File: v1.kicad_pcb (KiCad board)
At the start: 4 copper layers, 223.5 x 132.1 mm, 463 parts, among them CN1 ARJM11D7-502-AB-EW2, J1 Powerpole G1377G2, J10 Barrel_Jack, J11 USB_A, J2 Conn_01x02, J3 Conn_01x02, J4 Conn_01x02, J5 Conn_01x02, J6 Conn_01x02, J7 Conn_01x02, J8 Micro_SD_Card_Det, J9 USB_B_Micro, M1 Logo_10mmx10mm, Q1 Si7141DP, Q10 Si7141DP, Q11 SI1539CDL-T1-GE3, Q12 SI1539CDL-T1-GE3, Q13 SI1539CDL-T1-GE3, Q15 Si7141DP, Q16 SI1539CDL-T1-GE3, Q17 Si7141DP, Q18 SI1539CDL-T1-GE3, Q19 Si7141DP, Q2 SI1539CDL-T1-GE3, Q20 SI1539CDL-T1-GE3, Q21 SI1539CDL-T1-GE3, Q3 SI1539CDL-T1-GE3, Q5 Si7141DP, Q6 SI1539CDL-T1-GE3, Q7 Si7141DP, Q8 SI1539CDL-T1-GE3, SW1 SW_SPDT, SW2 SW_Push, T1 Transformer_SP_1S, U1 171050601, U10 74HC08BQ, U11 TLV803, U12 TLV803, U13 74HC74, U14 74HC74, U15 MAX9612, U16 74HC1G08, U17 TPS3701DDCR, U18 NCP1117-3.3_TO252, U19 74HC08BQ, U2 TLV803, U20 TLV803, U21 TLV803, U22 74HC74, U23 74HC74, U24 MAX9612, U25 74HC1G08, U26 TPS3701DDCR, U27 NCP1117-3.3_TO252, U28 TLV803S, U29 74HC08BQ, U3 TLV803, U30 TLV803, U31 TLV803, U32 74HC74, U33 74HC74, U34 MAX9612, U35 74HC1G08, U36 TPS3701DDCR, U37 TLV803, U38 TLV803, U39 74HC74, U4 74HC74, U40 74HC74, U41 MAX9612, U42 74HC1G08, U43 TPS3701DDCR, U44 LT3460, U45 TLV803, U46 TLV803, U47 74HC74, U48 74HC74, U49 MAX9612, U5 74HC74, U50 74HC1G08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

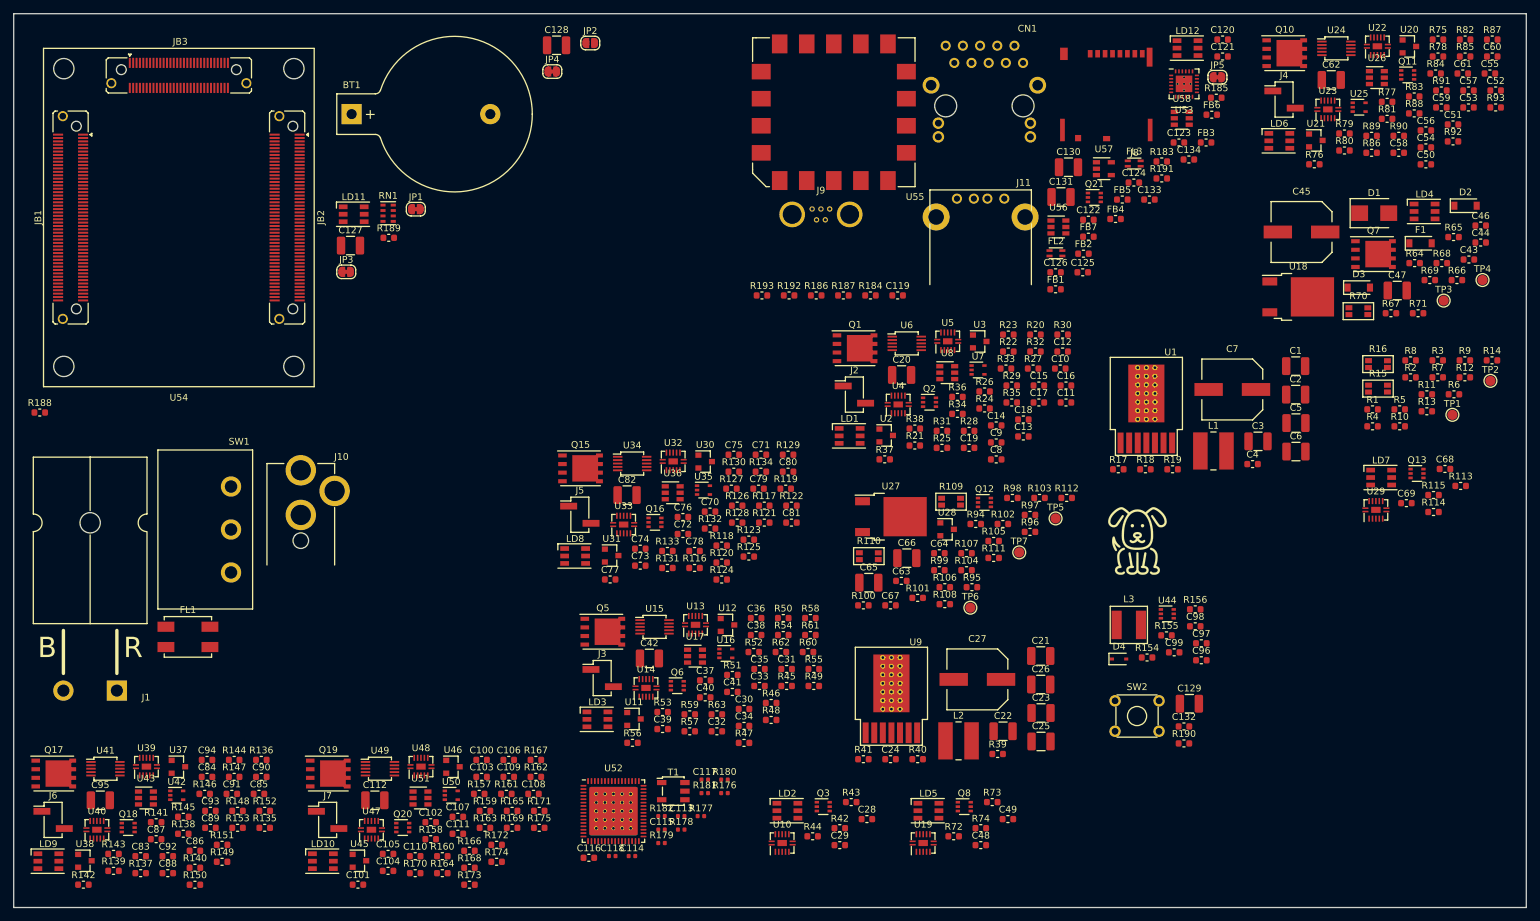
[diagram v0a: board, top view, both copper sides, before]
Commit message: Implemented FPGA based PMIC
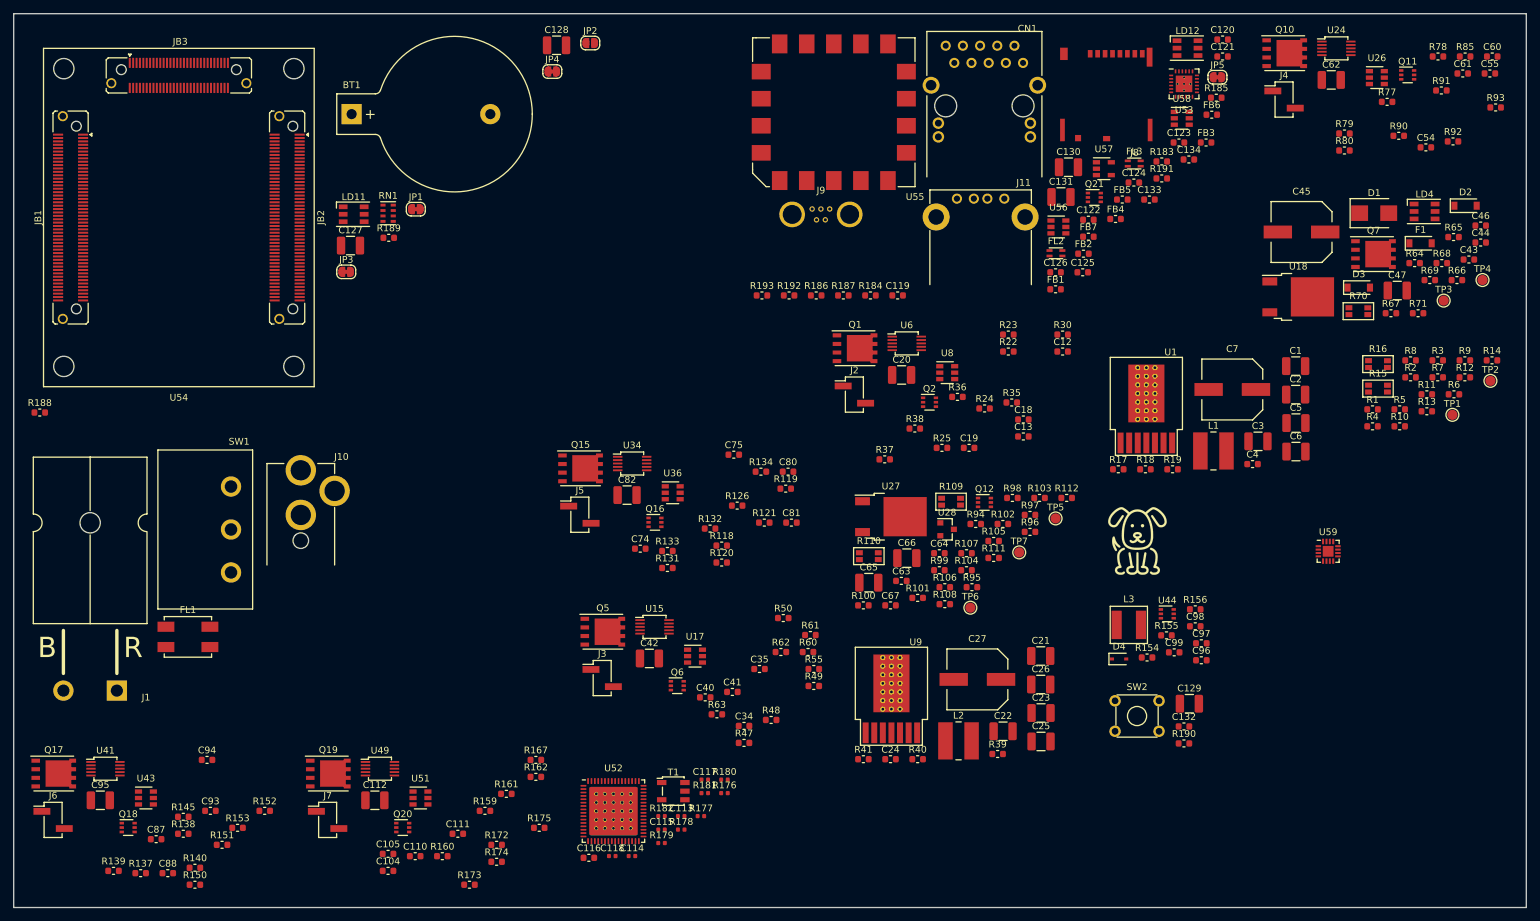
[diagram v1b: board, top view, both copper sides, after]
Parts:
- removed C10, C102, C103, C107, C109, C11, C15, C17, C29, C32, C33, C37, C39, C49, C52, C53, C57, C59, C69, C72, C73, C77, C79, C85, C86, C90, C92: 100n, Capacitor_SMD:C_0603_1608Metric
- removed C100, C101, C106, C14, C30, C31, C36, C50, C51, C56, C70, C71, C76, C8, C83, C84, C89, C9: 1u, Capacitor_SMD:C_0603_1608Metric
- removed C108, C16, C38, C58, C78, C91: 100nF, Capacitor_SMD:C_0603_1608Metric
- removed C28, C48, C68: 4u7, Capacitor_SMD:C_0603_1608Metric
- removed LD1, LD10, LD2, LD3, LD5, LD6, LD7, LD8, LD9: LED_Cree_CLX6E-FKC, LED_SMD:LED_RGB_PLCC-6
- removed Q13, Q3, Q8: SI1539CDL-T1-GE3, Package_TO_SOT_SMD:SOT-363_SC-70-6
- removed R113, R42, R72: 100k, Resistor_SMD:R_0603_1608Metric
- removed R114, R125, R144, R166, R29, R43, R54, R73, R84: 22k, Resistor_SMD:R_0603_1608Metric
- removed R115, R130, R149, R171, R34, R44, R59, R74, R89: 33k, Resistor_SMD:R_0603_1608Metric
- removed R116, R117, R122, R123, R127, R128, R129, R135, R136, R141, R142, R146, R147, R148, R157, R158, R163, R164, R168, R169, R170, R20, R21, R26, R27, R31, R32, R33, R45, R46, R51, R52, R56, R57, R58, R75, R76, R81, R82, R86, R87, R88: 47k, Resistor_SMD:R_0603_1608Metric
- removed R124, R143, R165, R28, R53, R83: 7k5, Resistor_SMD:R_0603_1608Metric
- removed U10, U19, U29: 74HC08BQ, IC_WUT:DHVQFN14_(SOT762-1)
- removed U11, U12, U2, U20, U21, U3, U30, U31, U37, U38, U45, U46: TLV803, Package_TO_SOT_SMD:SOT-23
- removed U13, U14, U22, U23, U32, U33, U39, U4, U40, U47, U48, U5: 74HC74, IC_WUT:DHVQFN14_(SOT762-1)
- removed U16, U25, U35, U42, U50, U7: 74HC1G08, Package_TO_SOT_SMD:SOT-353_SC-70-5
- added U59: AD5689RxCPZ, Package_CSP:LFCSP-16-1EP_3x3mm_P0.5mm_EP1.854x1.854mm, F.Cu at (242.5, 115.0)
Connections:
- R126 pad 2: /Power Supply/Stage 3 Regulators/1V8 Monitor/~Overcurrent -> /Power Supply/Stage 3 Regulators/1V8 Monitor/I_Good
- R134 pad 2: /Power Supply/Stage 3 Regulators/1V8 Monitor/~V_Fault -> /Power Supply/Stage 3 Regulators/1V8 Monitor/V_Good
- R145 pad 2: /Power Supply/Stage 3 Regulators/ADC 3V3 Monitor/~Overcurrent -> /Power Supply/Stage 3 Regulators/ADC 3V3 Monitor/I_Good
- R153 pad 2: /Power Supply/Stage 3 Regulators/ADC 3V3 Monitor/~V_Fault -> /Power Supply/Stage 3 Regulators/ADC 3V3 Monitor/V_Good
- R167 pad 2: /Power Supply/Stage 3 Regulators/16V Monitor/~Overcurrent -> /Power Supply/Stage 3 Regulators/16V Monitor/I_Good
- R175 pad 2: /Power Supply/Stage 3 Regulators/16V Monitor/~V_Fault -> /Power Supply/Stage 3 Regulators/16V Monitor/V_Good
- R30 pad 2: /Power Supply/Stage 2 Regulators/3V3 Monitor/~Overcurrent -> /Power Supply/Stage 2 Regulators/3V3 Monitor/I_Good
- R38 pad 2: /Power Supply/Stage 2 Regulators/3V3 Monitor/~V_Fault -> /Power Supply/Stage 2 Regulators/3V3 Monitor/V_Good
- R55 pad 2: /Power Supply/Stage 2 Regulators/5V Monitor/~Overcurrent -> /Power Supply/Stage 2 Regulators/5V Monitor/I_Good
- R63 pad 2: /Power Supply/Stage 2 Regulators/5V Monitor/~V_Fault -> /Power Supply/Stage 2 Regulators/5V Monitor/V_Good
- R85 pad 2: /Power Supply/Stage 1 Regulators/12V Monitor/~Overcurrent -> /Power Supply/Stage 1 Regulators/12V Monitor/I_Good
- R93 pad 2: /Power Supply/Stage 1 Regulators/12V Monitor/~V_Fault -> /Power Supply/Stage 1 Regulators/12V Monitor/V_Good
- U15 pad 1: /Power Supply/Stage 2 Regulators/5V Monitor/~Overcurrent -> /Power Supply/Stage 2 Regulators/5V Monitor/I_Good
- U17 pad 1: /Power Supply/Stage 2 Regulators/5V Monitor/~V_Fault -> /Power Supply/Stage 2 Regulators/5V Monitor/V_Good
- U17 pad 6: /Power Supply/Stage 2 Regulators/5V Monitor/~V_Fault -> /Power Supply/Stage 2 Regulators/5V Monitor/V_Good
- U24 pad 1: /Power Supply/Stage 1 Regulators/12V Monitor/~Overcurrent -> /Power Supply/Stage 1 Regulators/12V Monitor/I_Good
- U26 pad 1: /Power Supply/Stage 1 Regulators/12V Monitor/~V_Fault -> /Power Supply/Stage 1 Regulators/12V Monitor/V_Good
- U26 pad 6: /Power Supply/Stage 1 Regulators/12V Monitor/~V_Fault -> /Power Supply/Stage 1 Regulators/12V Monitor/V_Good
- U34 pad 1: /Power Supply/Stage 3 Regulators/1V8 Monitor/~Overcurrent -> /Power Supply/Stage 3 Regulators/1V8 Monitor/I_Good
- U36 pad 1: /Power Supply/Stage 3 Regulators/1V8 Monitor/~V_Fault -> /Power Supply/Stage 3 Regulators/1V8 Monitor/V_Good
- U36 pad 6: /Power Supply/Stage 3 Regulators/1V8 Monitor/~V_Fault -> /Power Supply/Stage 3 Regulators/1V8 Monitor/V_Good
- U41 pad 1: /Power Supply/Stage 3 Regulators/ADC 3V3 Monitor/~Overcurrent -> /Power Supply/Stage 3 Regulators/ADC 3V3 Monitor/I_Good
- U43 pad 1: /Power Supply/Stage 3 Regulators/ADC 3V3 Monitor/~V_Fault -> /Power Supply/Stage 3 Regulators/ADC 3V3 Monitor/V_Good
- U43 pad 6: /Power Supply/Stage 3 Regulators/ADC 3V3 Monitor/~V_Fault -> /Power Supply/Stage 3 Regulators/ADC 3V3 Monitor/V_Good
- U49 pad 1: /Power Supply/Stage 3 Regulators/16V Monitor/~Overcurrent -> /Power Supply/Stage 3 Regulators/16V Monitor/I_Good
- U51 pad 1: /Power Supply/Stage 3 Regulators/16V Monitor/~V_Fault -> /Power Supply/Stage 3 Regulators/16V Monitor/V_Good
- U51 pad 6: /Power Supply/Stage 3 Regulators/16V Monitor/~V_Fault -> /Power Supply/Stage 3 Regulators/16V Monitor/V_Good
- U6 pad 1: /Power Supply/Stage 2 Regulators/3V3 Monitor/~Overcurrent -> /Power Supply/Stage 2 Regulators/3V3 Monitor/I_Good
- U8 pad 1: /Power Supply/Stage 2 Regulators/3V3 Monitor/~V_Fault -> /Power Supply/Stage 2 Regulators/3V3 Monitor/V_Good
- U8 pad 6: /Power Supply/Stage 2 Regulators/3V3 Monitor/~V_Fault -> /Power Supply/Stage 2 Regulators/3V3 Monitor/V_Good
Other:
- net class Default: clearance 0.2 -> 0.0889
- rule trace_clearance: 0.2 -> 0.0889

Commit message: muppet hadn't saved everything :(
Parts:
- removed C104, C110, C87, C93, C96: 4u7, Capacitor_SMD:C_0603_1608Metric
- removed C105, C111, C123, C125, C126, C132, C134, C81, C88, C94: 100n, Capacitor_SMD:C_0603_1608Metric
- removed C112, C127, C128, C129, C82, C95: 22u, Capacitor_SMD:C_1210_3225Metric
- removed C113: 10n, Capacitor_SMD:C_0402_1005Metric
- removed C114: 100n, Capacitor_SMD:C_0402_1005Metric
- removed C115, C117, C118: 8p2, Capacitor_SMD:C_0402_1005Metric
- removed C116: 2u2, Capacitor_SMD:C_0603_1608Metric
- removed C119, C120, C121: 100nF, Capacitor_SMD:C_0603_1608Metric
- removed C122, C124, C133: 1u, Capacitor_SMD:C_0603_1608Metric
- removed C130, C131: 47u, Capacitor_SMD:C_1210_3225Metric
- removed C97: 47n, Capacitor_SMD:C_0603_1608Metric
- removed C98: 22p, Capacitor_SMD:C_0603_1608Metric
- removed C99: 22u, Capacitor_SMD:C_0603_1608Metric
- removed CN1: ARJM11D7-502-AB-EW2, Connector_WUT:Connector_RJ45_Magjack_Abracon_ARJM11D7-502-AB-EW2
- removed Q16, Q18, Q20, Q21: SI1539CDL-T1-GE3, Package_TO_SOT_SMD:SOT-363_SC-70-6
- removed Q17, Q19: Si7141DP, Package_SO:PowerPAK_SO-8_Single
- removed R151, R152, R173, R174, R183, R185, R190, R191: 10k, Resistor_SMD:R_0603_1608Metric
- removed R153, R154, R167, R175: 47k, Resistor_SMD:R_0603_1608Metric
- removed R155: 390k, Resistor_SMD:R_0603_1608Metric
- removed R156, R188, R192: 33k, Resistor_SMD:R_0603_1608Metric
- removed R159, R160, R161, R162: R, Resistor_SMD:R_0603_1608Metric
- removed R172: 100R, Resistor_SMD:R_0603_1608Metric
- removed R176, R177: 10R, Resistor_SMD:R_0402_1005Metric
- removed R178, R179: 35R, Resistor_SMD:R_0402_1005Metric
- removed R180, R181, R182: 5R1, Resistor_SMD:R_0402_1005Metric
- removed R184: 4k7, Resistor_SMD:R_0603_1608Metric
- removed R186, R187: 1k, Resistor_SMD:R_0603_1608Metric
- removed R189, R193: 22k, Resistor_SMD:R_0603_1608Metric
- removed U28: TLV803S, Package_TO_SOT_SMD:SOT-23
- removed U34, U41, U49: MAX9612, IC_WUT:uMAX-10_3x3mm_P0.5mm
- removed U36, U43, U51: TPS3701DDCR, Package_TO_SOT_SMD:SOT-23-6
- removed U44: LT3460, Package_TO_SOT_SMD:SOT-363_SC-70-6
- removed U52: LTC2216, IC_WUT:QFN-64-1EP_9x9mm_P0.5mm_EP7.15x7.15mm
- removed U53: TXS02612, IC_WUT:WQFN-24-1EP_4.1x4.1mm_P0.5mm_EP2.45x2.45mm
- removed U54: TE0720, IC_WUT:Trenz_TE0720
- removed U55: JTAG-SMT3, Misc_WUT:JTAG-SMT3-NC
- removed U56, U58: TPD2S017, Package_TO_SOT_SMD:SOT-23-6
- removed U57: TPS2051B, Package_TO_SOT_SMD:SOT-23-5
- removed U59: AD5689RxCPZ, Package_CSP:LFCSP-16-1EP_3x3mm_P0.5mm_EP1.854x1.854mm
- added C10: 100n, Capacitor_SMD:C_0603_1608Metric, F.Cu at (220.6, 112.9)
- added C11: 4u7, Capacitor_SMD:C_0603_1608Metric, F.Cu at (215.0, 117.6)
- added C14: 10u, Capacitor_SMD:C_1210_3225Metric, F.Cu at (156.0, 129.7)
- added C15: 10u, Capacitor_SMD:C_1210_3225Metric, F.Cu at (156.0, 138.1)
- added C16: 470n, Capacitor_SMD:C_0603_1608Metric, F.Cu at (129.8, 144.9)
- added C17: 22u, Capacitor_SMD:C_1210_3225Metric, F.Cu at (150.4, 140.8)
- added C28: 4u7, Capacitor_SMD:C_0603_1608Metric, F.Cu at (265.2, 47.8)
- added C29: 22u, Capacitor_SMD:C_1210_3225Metric, F.Cu at (252.8, 54.9)
- added C30: 4u7, Capacitor_SMD:C_0603_1608Metric, F.Cu at (190.6, 112.9)
- added C31: 100n, Capacitor_SMD:C_0603_1608Metric, F.Cu at (185.0, 120.1)
- added C32: 100n, Capacitor_SMD:C_0603_1608Metric, F.Cu at (185.0, 117.6)
- added C33: 4u7, Capacitor_SMD:C_0603_1608Metric, F.Cu at (186.5, 113.4)
- added C36: 4u7, Capacitor_SMD:C_0603_1608Metric, F.Cu at (198.8, 85.8)
- added C37: 22u, Capacitor_SMD:C_1210_3225Metric, F.Cu at (173.6, 98.3)
- added C38: 22u, Capacitor_SMD:C_1210_3225Metric, F.Cu at (179.2, 94.7)
- added C39: 100nF, Capacitor_SMD:C_0603_1608Metric, F.Cu at (172.8, 101.6)
- added C48: 4u7, Capacitor_SMD:C_0603_1608Metric, F.Cu at (72.1, 158.5)
- added C49: 22u, Capacitor_SMD:C_1210_3225Metric, F.Cu at (60.9, 154.4)
- added C50: 22p, Capacitor_SMD:C_0603_1608Metric, F.Cu at (147.4, 158.8)
- added C51: 4u7, Capacitor_SMD:C_0603_1608Metric, F.Cu at (147.4, 156.3)
- added C52: 22u, Capacitor_SMD:C_0603_1608Metric, F.Cu at (146.5, 153.8)
- added C53: 47n, Capacitor_SMD:C_0603_1608Metric, F.Cu at (143.4, 157.6)
- added C56: 100n, Capacitor_SMD:C_0603_1608Metric, F.Cu at (187.5, 138.9)
- added C57: 4u7, Capacitor_SMD:C_0603_1608Metric, F.Cu at (183.5, 141.5)
- added C58: 22u, Capacitor_SMD:C_1210_3225Metric, F.Cu at (176.3, 134.8)
- added C59: 2u2, Capacitor_SMD:C_0603_1608Metric, F.Cu at (210.4, 99.0)
- added C68: 100n, Capacitor_SMD:C_0603_1608Metric, F.Cu at (207.2, 130.7)
- added C69: 1u, Capacitor_SMD:C_0603_1608Metric, F.Cu at (178.7, 79.8)
- added C70: 100n, Capacitor_SMD:C_0603_1608Metric, F.Cu at (206.0, 77.0)
- added C71: 1u, Capacitor_SMD:C_0603_1608Metric, F.Cu at (224.4, 53.4)
- added C72: 100n, Capacitor_SMD:C_0603_1608Metric, F.Cu at (212.5, 65.6)
- added C73: 100nF, Capacitor_SMD:C_0603_1608Metric, F.Cu at (158.6, 79.8)
- added C76: 1u, Capacitor_SMD:C_0603_1608Metric, F.Cu at (166.7, 79.8)
- added C77: 100n, Capacitor_SMD:C_0603_1608Metric, F.Cu at (170.7, 79.8)
- added C78: 100n, Capacitor_SMD:C_0603_1608Metric, F.Cu at (174.7, 79.8)
- added C79: 47u, Capacitor_SMD:C_1210_3225Metric, F.Cu at (203.9, 60.8)
- added C8: 4u7, Capacitor_SMD:C_0603_1608Metric, F.Cu at (219.0, 115.9)
- added C9: 100n, Capacitor_SMD:C_0603_1608Metric, F.Cu at (215.0, 120.1)
- added J12: USB_A, Connector_WUT:USB-A_Wurth_61400416021_TH_RA, F.Cu at (190.9, 69.4)
- added J13: ARJM11D7-502-AB-EW2, Connector_WUT:Connector_RJ45_Magjack_Abracon_ARJM11D7-502-AB-EW2, F.Cu at (191.5, 52.8)
- added LD1: LED_Cree_CLX6E-FKC, LED_SMD:LED_RGB_PLCC-6, F.Cu at (256.9, 43.2)
- added LD10: LED_Cree_CLX6E-FKC, LED_SMD:LED_RGB_PLCC-6, F.Cu at (153.4, 109.6)
- added LD2: LED_Cree_CLX6E-FKC, LED_SMD:LED_RGB_PLCC-6, F.Cu at (140.3, 111.1)
- added LD3: LED_Cree_CLX6E-FKC, LED_SMD:LED_RGB_PLCC-6, F.Cu at (131.0, 120.4)
- added LD5: LED_Cree_CLX6E-FKC, LED_SMD:LED_RGB_PLCC-6, F.Cu at (140.3, 116.2)
- added LD6: LED_Cree_CLX6E-FKC, LED_SMD:LED_RGB_PLCC-6, F.Cu at (153.4, 104.6)
- added LD7: LED_Cree_CLX6E-FKC, LED_SMD:LED_RGB_PLCC-6, F.Cu at (146.7, 114.7)
- added LD8: LED_Cree_CLX6E-FKC, LED_SMD:LED_RGB_PLCC-6, F.Cu at (137.5, 121.2)
- added LD9: LED_Cree_CLX6E-FKC, LED_SMD:LED_RGB_PLCC-6, F.Cu at (147.0, 104.6)
- added Q13: Si7141DP, Package_SO:PowerPAK_SO-8_Single, F.Cu at (169.4, 130.9)
- added Q14: SI1539CDL-T1-GE3, Package_TO_SOT_SMD:SOT-363_SC-70-6, F.Cu at (175.4, 138.8)
- added Q3: Si7141DP, Package_SO:PowerPAK_SO-8_Single, F.Cu at (169.4, 149.1)
- added Q4: SI1539CDL-T1-GE3, Package_TO_SOT_SMD:SOT-363_SC-70-6, F.Cu at (175.4, 157.1)
- added Q8: SI1539CDL-T1-GE3, Package_TO_SOT_SMD:SOT-363_SC-70-6, F.Cu at (190.7, 86.4)
- added Q9: Si7141DP, Package_SO:PowerPAK_SO-8_Single, F.Cu at (84.0, 150.4)
- added R113: 7k5, Resistor_SMD:R_0603_1608Metric, F.Cu at (162.6, 110.9)
- added R114: 33k, Resistor_SMD:R_0603_1608Metric, F.Cu at (151.9, 113.4)
- added R115: 22k, Resistor_SMD:R_0603_1608Metric, F.Cu at (158.6, 105.8)
- added R116: 7k5, Resistor_SMD:R_0603_1608Metric, F.Cu at (158.6, 108.3)
- added R117: 33k, Resistor_SMD:R_0603_1608Metric, F.Cu at (145.4, 118.5)
- added R122: 7k5, Resistor_SMD:R_0603_1608Metric, F.Cu at (155.9, 115.9)
- added R123: 33k, Resistor_SMD:R_0603_1608Metric, F.Cu at (153.5, 118.4)
- added R124: 22k, Resistor_SMD:R_0603_1608Metric, F.Cu at (162.6, 108.3)
- added R125: 7k5, Resistor_SMD:R_0603_1608Metric, F.Cu at (154.7, 121.0)
- added R127: 22k, Resistor_SMD:R_0603_1608Metric, F.Cu at (162.6, 105.8)
- added R128: 33k, Resistor_SMD:R_0603_1608Metric, F.Cu at (158.6, 103.3)
- added R129: 33k, Resistor_SMD:R_0603_1608Metric, F.Cu at (159.9, 113.4)
- added R130: 4k7, Resistor_SMD:R_0603_1608Metric, F.Cu at (158.7, 121.0)
- added R135: 5R1, Resistor_SMD:R_0402_1005Metric, F.Cu at (227.6, 89.4)
- added R136: 35R, Resistor_SMD:R_0402_1005Metric, F.Cu at (221.2, 92.8)
- added R141: 22k, Resistor_SMD:R_0603_1608Metric, F.Cu at (51.9, 97.1)
- added R142: 10k, Resistor_SMD:R_0603_1608Metric, F.Cu at (207.2, 133.2)
- added R143: 10k, Resistor_SMD:R_0603_1608Metric, F.Cu at (202.0, 74.5)
- added R144: 4k7, Resistor_SMD:R_0603_1608Metric, F.Cu at (210.9, 69.3)
- added R146: 10k, Resistor_SMD:R_0603_1608Metric, F.Cu at (221.7, 58.4)
- added R147: 33k, Resistor_SMD:R_0603_1608Metric, F.Cu at (202.0, 79.5)
- added R148: 22k, Resistor_SMD:R_0603_1608Metric, F.Cu at (206.0, 74.5)
- added R149: 1k, Resistor_SMD:R_0603_1608Metric, F.Cu at (216.5, 65.6)
- added R20: 100R, Resistor_SMD:R_0603_1608Metric, F.Cu at (224.6, 113.3)
- added R21: 10k, Resistor_SMD:R_0603_1608Metric, F.Cu at (223.0, 115.8)
- added R26: 10k, Resistor_SMD:R_0603_1608Metric, F.Cu at (219.0, 118.4)
- added R27: R, Resistor_SMD:R_0603_1608Metric, F.Cu at (222.9, 108.3)
- added R28: R, Resistor_SMD:R_0603_1608Metric, F.Cu at (216.6, 113.4)
- added R29: 68k, Resistor_SMD:R_0603_1608Metric, F.Cu at (149.6, 144.2)
- added R31: 0R, Resistor_SMD:R_0603_1608Metric, F.Cu at (133.8, 144.9)
- added R32: 100R, Resistor_SMD:R_0603_1608Metric, F.Cu at (187.5, 154.6)
- added R33: 10k, Resistor_SMD:R_0603_1608Metric, F.Cu at (183.5, 157.2)
- added R34: 47k, Resistor_SMD:R_0603_1608Metric, F.Cu at (189.1, 152.1)
- added R42: 1M2, Resistor_SMD:R_0603_1608Metric, F.Cu at (255.9, 58.3)
- added R43: 10k, Resistor_SMD:R_0603_1608Metric, F.Cu at (265.2, 45.3)
- added R44: 12k, Resistor_SMD:R_0603_1608Metric, F.Cu at (255.4, 50.9)
- added R45: 33k, Resistor_SMD:R_0603_1608Metric, F.Cu at (261.2, 47.0)
- added R46: 33k, Resistor_SMD:R_0603_1608Metric, F.Cu at (251.9, 58.3)
- added R51: 47k, Resistor_SMD:R_0603_1608Metric, F.Cu at (193.0, 118.3)
- added R52: 47k, Resistor_SMD:R_0603_1608Metric, F.Cu at (193.0, 115.8)
- added R53: R, Resistor_SMD:R_0603_1608Metric, F.Cu at (193.0, 120.8)
- added R54: R, Resistor_SMD:R_0603_1608Metric, F.Cu at (194.6, 113.3)
- added R56: R, Resistor_SMD:R_0603_1608Metric, F.Cu at (194.6, 110.8)
- added R57: R, Resistor_SMD:R_0603_1608Metric, F.Cu at (192.9, 108.3)
- added R58: 10m, Resistor_WUT:R_Shunt_Vishay_WSK1206, F.Cu at (173.6, 94.4)
- added R59: 130k, Resistor_SMD:R_0603_1608Metric, F.Cu at (192.0, 94.6)
- added R72: 10k, Resistor_SMD:R_0603_1608Metric, F.Cu at (188.8, 99.0)
- added R73: 1k8, Resistor_SMD:R_0603_1608Metric, F.Cu at (197.4, 90.8)
- added R74: 22k, Resistor_SMD:R_0603_1608Metric, F.Cu at (184.0, 93.9)
- added R75: 30k, Resistor_SMD:R_0603_1608Metric, F.Cu at (194.8, 85.8)
- added R76: 1k, Resistor_SMD:R_0603_1608Metric, F.Cu at (188.0, 93.9)
- added R81: R, Resistor_SMD:R_0603_1608Metric, F.Cu at (98.2, 158.6)
- added R82: R, Resistor_SMD:R_0603_1608Metric, F.Cu at (103.7, 150.9)
- added R83: 10k, Resistor_SMD:R_0603_1608Metric, F.Cu at (102.1, 148.4)
- added R84: R, Resistor_SMD:R_0603_1608Metric, F.Cu at (95.7, 153.5)
- added R86: 100R, Resistor_SMD:R_0603_1608Metric, F.Cu at (65.7, 153.5)
- added R87: 10k, Resistor_SMD:R_0603_1608Metric, F.Cu at (72.0, 148.4)
- added R88: 47k, Resistor_SMD:R_0603_1608Metric, F.Cu at (64.1, 157.8)
- added R89: 47k, Resistor_SMD:R_0603_1608Metric, F.Cu at (69.7, 153.1)
- added U10: NCP1117-3.3_TO252, Package_TO_SOT_SMD:TO-252-2, F.Cu at (176.8, 88.5)
- added U11: TLV803S, Package_TO_SOT_SMD:SOT-23, F.Cu at (185.2, 90.4)
- added U12: MAX9612, IC_WUT:uMAX-10_3x3mm_P0.5mm, F.Cu at (91.7, 149.7)
- added U13: TPS3701DDCR, Package_TO_SOT_SMD:SOT-23-6, F.Cu at (97.6, 149.5)
- added U14: MAX9612, IC_WUT:uMAX-10_3x3mm_P0.5mm, F.Cu at (61.6, 149.7)
- added U16: LT3460, Package_TO_SOT_SMD:SOT-363_SC-70-6, F.Cu at (142.4, 151.9)
- added U19: LCMXO2-640HC-4SG48C, Package_DFN_QFN:QFN-48-1EP_7x7mm_P0.5mm_EP5.3x5.3mm_ThermalVias, F.Cu at (132.4, 113.2)
- added U2: MAX9612, IC_WUT:uMAX-10_3x3mm_P0.5mm, F.Cu at (212.5, 109.6)
- added U20: LTC2216, IC_WUT:QFN-64-1EP_9x9mm_P0.5mm_EP7.15x7.15mm, F.Cu at (214.1, 92.1)
- added U21: TE0720, IC_WUT:Trenz_TE0720, F.Cu at (72.5, 68.3)
- added U22: JTAG-SMT3, Misc_WUT:JTAG-SMT3-NC, F.Cu at (169.2, 52.7)
- added U23: TPD2S017, Package_TO_SOT_SMD:SOT-23-6, F.Cu at (202.4, 70.9)
- added U25: TPS2051B, Package_TO_SOT_SMD:SOT-23-5, F.Cu at (209.2, 61.1)
- added U3: TPS3701DDCR, Package_TO_SOT_SMD:SOT-23-6, F.Cu at (218.5, 109.3)
- added U4: 171050601, Regulator_WUT:Wurth_171050601_TO263-7EP_EP6.4x8.54mm, F.Cu at (133.9, 133.7)
- added U5: MAX9612, IC_WUT:uMAX-10_3x3mm_P0.5mm, F.Cu at (177.0, 148.4)
- added U7: NCP1117-3.3_TO252, Package_TO_SOT_SMD:TO-252-2, F.Cu at (238.2, 55.9)
- C12, C18, C34, C44: value 4u7 -> 22u; footprint Capacitor_SMD:C_0603_1608Metric -> Capacitor_SMD:C_1210_3225Metric
- C13: value 100n -> 10u; footprint Capacitor_SMD:C_0603_1608Metric -> Capacitor_SMD:C_1210_3225Metric
- C19: value 100n -> 220u; footprint Capacitor_SMD:C_0603_1608Metric -> Capacitor_WUT:Wurth_WCAP_PSHP
- C20: value 22u -> 4u7; footprint Capacitor_SMD:C_1210_3225Metric -> Capacitor_SMD:C_0603_1608Metric
- C21, C22: value 10u -> 100n; footprint Capacitor_SMD:C_1210_3225Metric -> Capacitor_SMD:C_0603_1608Metric
- C23: value 10u -> 4u7; footprint Capacitor_SMD:C_1210_3225Metric -> Capacitor_SMD:C_0603_1608Metric
- C24: value 470n -> 22u; footprint Capacitor_SMD:C_0603_1608Metric -> Capacitor_SMD:C_1210_3225Metric
- C25: value 22u -> 220u; footprint Capacitor_SMD:C_1210_3225Metric -> Capacitor_WUT:Wurth_WCAP_PSHP
- C26: value 22u -> 47n; footprint Capacitor_SMD:C_1210_3225Metric -> Capacitor_SMD:C_0603_1608Metric
- C27, C45: value 220u -> 4u7; footprint Capacitor_WUT:Wurth_WCAP_PSHP -> Capacitor_SMD:C_0603_1608Metric
- C35: value 100n -> 4u7
- C42, C47: value 22u -> 100n; footprint Capacitor_SMD:C_1210_3225Metric -> Capacitor_SMD:C_0603_1608Metric
- C43: value 47n -> 4u7
- C46: value 4u7 -> 100n
- C60, C64: value 4u7 -> 8p2; footprint Capacitor_SMD:C_0603_1608Metric -> Capacitor_SMD:C_0402_1005Metric
- C61: value 100n -> 10n; footprint Capacitor_SMD:C_0603_1608Metric -> Capacitor_SMD:C_0402_1005Metric
- C62: value 22u -> 8p2; footprint Capacitor_SMD:C_1210_3225Metric -> Capacitor_SMD:C_0402_1005Metric
- C63: value 4u7 -> 100n; footprint Capacitor_SMD:C_0603_1608Metric -> Capacitor_SMD:C_0402_1005Metric
- C67: value 100nF -> 22u; footprint Capacitor_SMD:C_0603_1608Metric -> Capacitor_SMD:C_1210_3225Metric
- C74: value 4u7 -> 100nF
- C75: value 100n -> 100nF
- C80: value 4u7 -> 47u; footprint Capacitor_SMD:C_0603_1608Metric -> Capacitor_SMD:C_1210_3225Metric
- D1: value SMAJ24A -> MM3Z15VT1G; footprint Diode_SMD:D_SMB -> Diode_SMD:D_SOD-123
- D2: value MM3Z15VT1G -> SMAJ24A; footprint Diode_SMD:D_SOD-123 -> Diode_SMD:D_SMB
- J10: value Barrel_Jack -> USB_B_Micro; footprint Connector_WUT:Barrel-Jack_Cliff_FC681478_TH -> Connector_WUT:Micro-USB_Amphenol_MUSB-K152-30_Horizontal_TH
- J11: value USB_A -> Micro_SD_Card_Det; footprint Connector_WUT:USB-A_Wurth_61400416021_TH_RA -> Connector_WUT:Micro-SD_Molex_503398-1892
- J2: value Conn_01x02 -> Barrel_Jack; footprint Connector_PinHeader_2.54mm:PinHeader_1x02_P2.54mm_Vertical_SMD_Pin1Left -> Connector_WUT:Barrel-Jack_Cliff_FC681478_TH
- J8: value Micro_SD_Card_Det -> Conn_01x02; footprint Connector_WUT:Micro-SD_Molex_503398-1892 -> Connector_PinHeader_2.54mm:PinHeader_1x02_P2.54mm_Vertical_SMD_Pin1Left
- J9: value USB_B_Micro -> Conn_01x06_Male; footprint Connector_WUT:Micro-USB_Amphenol_MUSB-K152-30_Horizontal_TH -> Connector_JST:JST_PH_B6B-PH-K_1x06_P2.00mm_Vertical
- JP2: value SolderJumper_2_Open -> SolderJumper_2_Bridged; footprint Jumper:SolderJumper-2_P1.3mm_Open_RoundedPad1.0x1.5mm -> Jumper:SolderJumper-2_P1.3mm_Bridged_RoundedPad1.0x1.5mm
- JP3: value SolderJumper_2_Bridged -> SolderJumper_2_Open; footprint Jumper:SolderJumper-2_P1.3mm_Bridged_RoundedPad1.0x1.5mm -> Jumper:SolderJumper-2_P1.3mm_Open_RoundedPad1.0x1.5mm
- Q10, Q15, Q7: value Si7141DP -> SI1539CDL-T1-GE3; footprint Package_SO:PowerPAK_SO-8_Single -> Package_TO_SOT_SMD:SOT-363_SC-70-6
- Q11, Q6: value SI1539CDL-T1-GE3 -> Si7141DP; footprint Package_TO_SOT_SMD:SOT-363_SC-70-6 -> Package_SO:PowerPAK_SO-8_Single
- R1: value 10k -> 10m; footprint Resistor_SMD:R_0603_1608Metric -> Resistor_WUT:R_Shunt_Vishay_WSK1206
- R10: value 36k5 -> 36k
- R100: value 1M2 -> 47k
- R101: value 1k8 -> 47k
- R102: value 30k -> R
- R103, R105: value 33k -> R
- R104: value 330 -> 10k
- R106: value 680 -> R
- R107: value 22k -> 7k5
- R108, R14: value 1k -> 33k
- R109: value 10m -> 22k; footprint Resistor_WUT:R_Shunt_Vishay_WSK1206 -> Resistor_SMD:R_0603_1608Metric
- R11: value 33k -> 6k8
- R110: value 50m -> 7k5; footprint Resistor_WUT:R_Shunt_Vishay_WSK1206 -> Resistor_SMD:R_0603_1608Metric
- R111: value 1R -> 33k
- R112: value 10k -> 22k
- R118, R121: value R -> 22k
- R119: value R -> 7k5
- R12: value 1k -> 430k
- R120, R140, R48: value R -> 33k
- R126: value 47k -> 33k
- R13: value 33k -> 2k26
- R131: value 100R -> 4k7
- R133: value 10k -> 5R1; footprint Resistor_SMD:R_0603_1608Metric -> Resistor_SMD:R_0402_1005Metric
- R134: value 47k -> 10R; footprint Resistor_SMD:R_0603_1608Metric -> Resistor_SMD:R_0402_1005Metric
- R137: value R -> 35R; footprint Resistor_SMD:R_0603_1608Metric -> Resistor_SMD:R_0402_1005Metric
- R138: value R -> 10R; footprint Resistor_SMD:R_0603_1608Metric -> Resistor_SMD:R_0402_1005Metric
- R139: value R -> 5R1; footprint Resistor_SMD:R_0603_1608Metric -> Resistor_SMD:R_0402_1005Metric
- R145, R30, R38, R55: value 47k -> 10k
- R15: value 10m -> 36k5; footprint Resistor_WUT:R_Shunt_Vishay_WSK1206 -> Resistor_SMD:R_0603_1608Metric
- R150: value 100R -> 1k
- R16: value 10m -> 1k; footprint Resistor_WUT:R_Shunt_Vishay_WSK1206 -> Resistor_SMD:R_0603_1608Metric
- R2: value 3k16 -> 10k
- R22, R23, R79, R80: value R -> 47k
- R3: value 36k -> 3k16
- R35: value 100R -> 47k
- R36, R37, R40, R91: value 10k -> R
- R39: value 68k -> R
- R4: value 6k8 -> 330k
- R41: value 0R -> 10m; footprint Resistor_SMD:R_0603_1608Metric -> Resistor_WUT:R_Shunt_Vishay_WSK1206
- R47: value R -> 470
- R49, R77: value R -> 100R
- R5: value 330k -> 2k74
- R50, R78: value R -> 10k
- R6: value 2k74 -> 33k
- R60: value 100R -> 2k2
- R61: value 10k -> 33k
- R62: value 10k -> 36k
- R63: value 47k -> 330
- R64: value 10k -> 50m; footprint Resistor_SMD:R_0603_1608Metric -> Resistor_WUT:R_Shunt_Vishay_WSK1206
- R65: value 1M2 -> 330k
- R66: value 12k -> 2k74
- R68: value 33k -> 44k2
- R69: value 470 -> 680
- R70: value 10m -> 1R; footprint Resistor_WUT:R_Shunt_Vishay_WSK1206 -> Resistor_SMD:R_0603_1608Metric
- R71: value 33k -> 1M2
- R8: value 430k -> 1k
- R85, R93: value 47k -> R
- R9: value 2k26 -> 10m; footprint Resistor_SMD:R_0603_1608Metric -> Resistor_WUT:R_Shunt_Vishay_WSK1206
- R90: value 100R -> R
- R94: value 130k -> R
- R95: value 2k2 -> 390k
- R96: value 36k -> 47k
- R97: value 330k -> 33k
- R98: value 2k74 -> 100R
- R99: value 44k2 -> 10k
- TP3: value 3V3 LP -> V In
- TP4: value V In -> 3V3 LP
- U15, U6: value MAX9612 -> TPS3701DDCR; footprint IC_WUT:uMAX-10_3x3mm_P0.5mm -> Package_TO_SOT_SMD:SOT-23-6
- U17, U8: value TPS3701DDCR -> MAX9612; footprint Package_TO_SOT_SMD:SOT-23-6 -> IC_WUT:uMAX-10_3x3mm_P0.5mm
- U18: value NCP1117-3.3_TO252 -> TPS3701DDCR; footprint Package_TO_SOT_SMD:TO-252-2 -> Package_TO_SOT_SMD:SOT-23-6
- U24: value MAX9612 -> TXS02612; footprint IC_WUT:uMAX-10_3x3mm_P0.5mm -> IC_WUT:WQFN-24-1EP_4.1x4.1mm_P0.5mm_EP2.45x2.45mm
- U26: value TPS3701DDCR -> TPD2S017
- U27: value NCP1117-3.3_TO252 -> AD5689RxCPZ; footprint Package_TO_SOT_SMD:TO-252-2 -> Package_CSP:LFCSP-16-1EP_3x3mm_P0.5mm_EP1.854x1.854mm
- U9: value 171050601 -> TPS3701DDCR; footprint Regulator_WUT:Wurth_171050601_TO263-7EP_EP6.4x8.54mm -> Package_TO_SOT_SMD:SOT-23-6
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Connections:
- net Net-(LD4-Pad4) renamed /Power Supply/Power Rail Management/5V_IFault
- net Net-(LD4-Pad6) renamed /Power Supply/Power Rail Management/5V_VFault
- C12 pad 1: 3V3_LP -> +3V3
- C13 pad 1: 3V3_LP -> /Power Supply/Stage 2 Regulators/12V_In
- C18 pad 1: /Power Supply/Stage 2 Regulators/3V3 Monitor/Vin -> /Power Supply/Stage 2 Regulators/5V_5A Regulator/Vout
- C19 pad 1: Net-(C19-Pad1) -> /Power Supply/Stage 2 Regulators/5V_5A Regulator/Vout
- C20 pad 1: +3V3 -> 3V3_LP
- C21 pad 1: /Power Supply/Stage 2 Regulators/12V_In -> 3V3_LP
- C23 pad 1: Net-(C22-Pad1) -> /Power Supply/Stage 2 Regulators/5V Monitor/Vin
- C24 pad 1: Net-(C24-Pad1) -> +5V
- C25 pad 1: /Power Supply/Stage 2 Regulators/5V_5A Regulator/Vout -> Net-(C25-Pad1)
- C26 pad 1: /Power Supply/Stage 2 Regulators/5V_5A Regulator/Vout -> Net-(C26-Pad1)
- C27 pad 1: /Power Supply/Stage 2 Regulators/5V_5A Regulator/Vout -> Net-(C27-Pad1)
- C34 pad 1: 3V3_LP -> /Power Supply/Stage 2 Regulators/12V_In
- C35 pad 1: 3V3_LP -> +5V
- C40 pad 1: /Power Supply/Stage 2 Regulators/5V Monitor/Vin -> 3V3_LP
- C41 pad 1: Net-(C41-Pad1) -> 3V3_LP
- C42 pad 1: +5V -> Net-(C42-Pad1)
- C43 pad 1: Net-(C43-Pad1) -> /Power Supply/Stage 3 Regulators/1V8 Monitor/Vin
- C44 pad 1: Net-(C44-Pad1) -> +1V8
- C45 pad 1: Net-(C44-Pad1) -> 3V3_LP
- C46 pad 1: Net-(C46-Pad1) -> 3V3_LP
- C47 pad 1: 3V3_LP -> Net-(C47-Pad1)
- C60 pad 1: /Power Supply/Stage 1 Regulators/12V Monitor/Vin -> Net-(C60-Pad1)
- C61 pad 1: Net-(C61-Pad1) -> GND
- C61 pad 2: GND -> Net-(C61-Pad2)
- C62 pad 1: /Power Supply/Stage 2 Regulators/12V_In -> Net-(C60-Pad1)
- C62 pad 2: GND -> Net-(C62-Pad2)
- C63 pad 1: +5V -> Net-(C61-Pad2)
- C64 pad 1: Net-(C64-Pad1) -> Net-(C62-Pad2)
- C65 pad 1: Net-(C64-Pad1) -> +3V3
- C66 pad 1: Net-(C64-Pad1) -> +3V3
- C67 pad 1: S3_PWR_ENABLE -> +3V3
- C74 pad 1: 3V3_LP -> Net-(C74-Pad1)
- C75 pad 1: 3V3_LP -> Net-(C75-Pad1)
- C80 pad 1: /Power Supply/Stage 3 Regulators/1V8 Monitor/Vin -> Net-(C79-Pad1)
- D1 pad 1: /Power Supply/Stage 1 Regulators/Vin -> Net-(C25-Pad1)
- D1 pad 2: GND -> Net-(C26-Pad1)
- D2 pad 1: Net-(C44-Pad1) -> /Power Supply/Stage 1 Regulators/Vin
- D2 pad 2: Net-(C43-Pad1) -> GND
- F1 pad 2: Net-(C46-Pad1) -> Net-(C27-Pad1)
- FB1 pad 1: +1V8 -> +3V3
- FB1 pad 2: Net-(C119-Pad1) -> Net-(FB1-Pad2)
- FB3 pad 1: +3V3 -> +1V8
- FB3 pad 2: Net-(FB3-Pad2) -> Net-(C73-Pad1)
- FB4 pad 1: +3V3 -> Net-(C71-Pad1)
- FB4 pad 2: Net-(C121-Pad1) -> Net-(FB4-Pad2)
- FB5 pad 1: Net-(C124-Pad1) -> +3V3
- FB5 pad 2: Net-(FB5-Pad2) -> Net-(C75-Pad1)
- FB6 pad 1: Net-(FB6-Pad1) -> +3V3
- FB6 pad 2: Net-(C130-Pad1) -> Net-(C76-Pad1)
- FB7 pad 1: +3V3 -> Net-(FB7-Pad1)
- FB7 pad 2: Net-(C133-Pad1) -> Net-(C79-Pad1)
- J10 pad 1: Net-(J1-Pad1) -> Net-(FB4-Pad2)
- J10 pad 2: Net-(FL1-Pad3) -> Net-(FL2-Pad2)
- J10 pad 3: (no net) -> Net-(FL2-Pad4)
- J11 pad 1: Net-(C130-Pad1) -> Net-(J11-Pad1)
- J11 pad 4: GND -> Net-(C75-Pad1)
- J11 pad 5: GND -> Net-(J11-Pad5)
- J2 pad 1: /Power Supply/Stage 2 Regulators/3V3 Monitor/Sense+ -> Net-(J1-Pad1)
- J2 pad 2: /Power Supply/Stage 2 Regulators/3V3 Monitor/Sense- -> Net-(FL1-Pad3)
- J3 pad 1: /Power Supply/Stage 2 Regulators/5V Monitor/Sense+ -> /Power Supply/Stage 2 Regulators/3V3 Monitor/Sense+
- J3 pad 2: /Power Supply/Stage 2 Regulators/5V Monitor/Sense- -> /Power Supply/Stage 2 Regulators/3V3 Monitor/Sense-
- J4 pad 1: /Power Supply/Stage 1 Regulators/12V Monitor/Sense+ -> /Power Supply/Stage 2 Regulators/5V Monitor/Sense+
- J4 pad 2: /Power Supply/Stage 1 Regulators/12V Monitor/Sense- -> /Power Supply/Stage 2 Regulators/5V Monitor/Sense-
- J5 pad 1: /Power Supply/Stage 3 Regulators/1V8 Monitor/Sense+ -> /Power Supply/Stage 1 Regulators/12V Monitor/Sense+
- J5 pad 2: /Power Supply/Stage 3 Regulators/1V8 Monitor/Sense- -> /Power Supply/Stage 1 Regulators/12V Monitor/Sense-
- J6 pad 1: /Power Supply/Stage 3 Regulators/ADC 3V3 Monitor/Sense+ -> /Power Supply/Stage 3 Regulators/1V8 Monitor/Sense+
- J6 pad 2: /Power Supply/Stage 3 Regulators/ADC 3V3 Monitor/Sense- -> /Power Supply/Stage 3 Regulators/1V8 Monitor/Sense-
- J7 pad 1: /Power Supply/Stage 3 Regulators/16V Step-up Regulator/16V_Out -> /Power Supply/Stage 3 Regulators/ADC 3V3 Monitor/Sense+
- J7 pad 2: /Power Supply/Stage 3 Regulators/16V Monitor/Sense- -> /Power Supply/Stage 3 Regulators/ADC 3V3 Monitor/Sense-
- J8 pad 1: Net-(J8-Pad1) -> /Power Supply/Stage 3 Regulators/16V Step-up Regulator/16V_Out
- J8 pad 2: Net-(J8-Pad2) -> /Power Supply/Stage 3 Regulators/16V Monitor/Sense-
- J9 pad 1: Net-(FB5-Pad2) -> /Power Supply/Power Rail Management/JTAGEN
- J9 pad 2: Net-(FL2-Pad2) -> Net-(J9-Pad2)
- J9 pad 3: Net-(FL2-Pad4) -> Net-(J9-Pad3)
- J9 pad 5: GND -> Net-(J9-Pad5)
- JP1 pad 1: /FPGA/JB1/NOSEQ -> /FPGA/JB1/JTAGMODE
- JP2 pad 1: /FPGA/JB1/EN1 -> /FPGA/JB1/NOSEQ
- JP3 pad 1: /FPGA/JB1/MODE -> /FPGA/JB1/EN1
- JP4 pad 1: /FPGA/JB1/JTAGMODE -> /FPGA/JB1/MODE
- L2 pad 2: Net-(C22-Pad1) -> Net-(C14-Pad1)
- LD4 pad 2: GND -> Net-(LD4-Pad2)
- LD4 pad 5: Net-(LD4-Pad5) -> /Power Supply/Power Rail Management/5V_OK
- Q10 pad 1: /Power Supply/Stage 1 Regulators/12V Monitor/Vin -> GND
- Q10 pad 2: /Power Supply/Stage 1 Regulators/12V Monitor/Vin -> S3_PWR_ENABLE
- Q10 pad 3: /Power Supply/Stage 1 Regulators/12V Monitor/Vin -> Net-(Q10-Pad3)
- Q10 pad 5: /Power Supply/Stage 2 Regulators/12V_In -> Net-(Q10-Pad5)
- Q11 pad 1: GND -> /Power Supply/Stage 3 Regulators/ADC 3V3 Monitor/Vin
- Q11 pad 2: S1_PWR_ENABLE -> /Power Supply/Stage 3 Regulators/ADC 3V3 Monitor/Vin
- Q11 pad 3: Net-(Q11-Pad3) -> /Power Supply/Stage 3 Regulators/ADC 3V3 Monitor/Vin
- Q11 pad 5: Net-(Q11-Pad5) -> +3.3VADC
- Q12 pad 2: /Power Supply/Stage 3 Regulators/16V_Good -> S3_PWR_ENABLE
- Q12 pad 3: /Power Supply/Stage 3 Regulators/Backlight_Enable -> Net-(Q12-Pad3)
- Q12 pad 4: 3V3_LP -> Net-(Q12-Pad4)
- Q12 pad 6: Net-(Q12-Pad5) -> Net-(Q11-Pad4)
- Q15 pad 1: /Power Supply/Stage 3 Regulators/1V8 Monitor/Vin -> GND
- Q15 pad 2: /Power Supply/Stage 3 Regulators/1V8 Monitor/Vin -> Net-(C73-Pad1)
- Q15 pad 3: /Power Supply/Stage 3 Regulators/1V8 Monitor/Vin -> Net-(C74-Pad1)
- Q15 pad 4: Net-(Q15-Pad4) -> Net-(FB1-Pad2)
- Q15 pad 5: +1V8 -> Net-(Q15-Pad5)
- Q5 pad 1: /Power Supply/Stage 2 Regulators/5V Monitor/Vin -> Net-(C25-Pad1)
- Q5 pad 2: /Power Supply/Stage 2 Regulators/5V Monitor/Vin -> Net-(C25-Pad1)
- Q5 pad 3: /Power Supply/Stage 2 Regulators/5V Monitor/Vin -> Net-(C25-Pad1)
- Q5 pad 4: Net-(Q5-Pad4) -> Net-(C26-Pad1)
- Q5 pad 5: +5V -> /Power Supply/Stage 1 Regulators/Vin
- Q6 pad 1: GND -> /Power Supply/Stage 1 Regulators/12V Monitor/Vin
- Q6 pad 2: S2_PWR_ENABLE -> /Power Supply/Stage 1 Regulators/12V Monitor/Vin
- Q6 pad 3: Net-(Q6-Pad3) -> /Power Supply/Stage 1 Regulators/12V Monitor/Vin
- Q6 pad 5: Net-(Q6-Pad5) -> /Power Supply/Stage 2 Regulators/12V_In
- Q7 pad 1: Net-(C44-Pad1) -> GND
- Q7 pad 2: Net-(C44-Pad1) -> S1_PWR_ENABLE
- Q7 pad 3: Net-(C44-Pad1) -> Net-(Q7-Pad3)
- Q7 pad 4: Net-(C43-Pad1) -> Net-(Q7-Pad4)
- Q7 pad 5: /Power Supply/Stage 1 Regulators/Vin -> Net-(Q7-Pad5)
- R1 pad 2: /Power Supply/Stage 2 Regulators/3V3_5A Regulator/FB -> /Power Supply/Stage 2 Regulators/3V3 Monitor/Sense+
- R10 pad 1: /Power Supply/Stage 2 Regulators/5V Monitor/INb -> /Power Supply/Stage 2 Regulators/5V_5A Regulator/Vout
- R10 pad 2: GND -> /Power Supply/Stage 2 Regulators/5V_5A Regulator/FB
- R100 pad 1: /Power Supply/Stage 3 Regulators/16V Monitor/Sense- -> Net-(C56-Pad1)
- R100 pad 2: /Power Supply/Stage 3 Regulators/16V Monitor/INa -> 16V_V_Good
- R101 pad 1: /Power Supply/Stage 3 Regulators/16V Monitor/INa -> 3V3_LP
- R101 pad 2: /Power Supply/Stage 3 Regulators/16V Monitor/INb -> 16V_I_Good
- R102 pad 1: /Power Supply/Stage 3 Regulators/16V Monitor/INb -> 3V3_LP
- R102 pad 2: GND -> Net-(R102-Pad2)
- R103 pad 2: /Power Supply/Stage 3 Regulators/1V8 Monitor/SetV -> Net-(R103-Pad2)
- R104 pad 1: /Power Supply/Stage 3 Regulators/1V8 Monitor/SetV -> /Power Supply/Stage 3 Regulators/Backlight_Enable
- R105 pad 1: 3V3_LP -> Net-(R102-Pad2)
- R105 pad 2: /Power Supply/Stage 3 Regulators/ADC 3V3 Monitor/SetV -> GND
- R106 pad 1: /Power Supply/Stage 3 Regulators/ADC 3V3 Monitor/SetV -> Net-(R103-Pad2)
- R107 pad 1: 3V3_LP -> Net-(LD2-Pad1)
- R107 pad 2: /Power Supply/Stage 3 Regulators/16V Monitor/SetV -> GND
- R108 pad 1: /Power Supply/Stage 3 Regulators/16V Monitor/SetV -> Net-(LD2-Pad2)
- R109 pad 1: 1V8_from_FPGA -> Net-(LD2-Pad3)
- R109 pad 2: /Power Supply/Stage 3 Regulators/1V8 Monitor/Sense+ -> GND
- R11 pad 1: 3V3_LP -> /Power Supply/Stage 2 Regulators/5V_5A Regulator/FB
- R11 pad 2: /Power Supply/Stage 2 Regulators/3V3 Monitor/SetV -> /Power Supply/Stage 2 Regulators/5V_5A Regulator/FB_Gnd
- R110 pad 1: Net-(C64-Pad1) -> Net-(LD3-Pad1)
- R110 pad 2: /Power Supply/Stage 3 Regulators/ADC 3V3 Monitor/Sense+ -> GND
- R111 pad 1: /Power Supply/Stage 3 Regulators/16V Step-up Regulator/16V_Out -> Net-(LD3-Pad2)
- R111 pad 2: /Power Supply/Stage 3 Regulators/16V Monitor/Sense- -> GND
- R112 pad 1: 3V3_LP -> Net-(LD3-Pad3)
- R112 pad 2: Net-(Q12-Pad5) -> GND
- R118 pad 1: 3V3_LP -> Net-(LD5-Pad3)
- R118 pad 2: Net-(R118-Pad2) -> GND
- R119 pad 1: Net-(R118-Pad2) -> Net-(LD6-Pad1)
- R12 pad 1: /Power Supply/Stage 2 Regulators/3V3 Monitor/SetV -> /Power Supply/Stage 2 Regulators/5V Monitor/Vin
- R12 pad 2: GND -> /Power Supply/Stage 2 Regulators/5V Monitor/INa
- R120 pad 1: 3V3_LP -> Net-(LD6-Pad2)
- R120 pad 2: Net-(R120-Pad2) -> GND
- R121 pad 1: Net-(R120-Pad2) -> Net-(LD6-Pad3)
- R126 pad 1: 3V3_LP -> Net-(LD8-Pad2)
- R126 pad 2: /Power Supply/Stage 3 Regulators/1V8 Monitor/I_Good -> GND
- R13 pad 1: 3V3_LP -> /Power Supply/Stage 2 Regulators/5V Monitor/INa
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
